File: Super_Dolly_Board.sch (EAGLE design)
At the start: 101 parts, among them J1 10118193-0001LF, J3 SJ1-2503A, J4 RJHSE-5381, J5 SJ1-2503A, J6 SJ1-2503A, P1 TC33X-2, SW1 SKQUDBE010, U1 AT90USB646-MU, U10 IP4234CZ6, U11 AT90USB646-AU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

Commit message: working on SDB REV4
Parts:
- added AUX_2: (no value), PP_Connectors:PH_1X081.27MM_PTH
- R3, R32, R6: value 10K -> 4.7K
- U$1: REVNUM 3 -> 4
- renumbered AUX to AUX_1
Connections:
- new net N$2: AUX_2.3
- net +5V: now also AUX_2.1
- net GND: now also AUX_2.2; no longer CG10.1
- net M0_A: now also U1.PA0(AD0), U11.PA0(AD0); no longer U1.PA3(AD3), U11.PA3(AD3)
- net M0_B: now also U1.PA1(AD1), U11.PA1(AD1); no longer U1.PA4(AD4), U11.PA4(AD4)
- net M0_P: now also U1.PA2(AD2), U11.PA2(AD2); no longer U1.PA0(AD0), U11.PA0(AD0)
- net M1_A: now also U1.PA3(AD3), U11.PA3(AD3); no longer U1.PA5(AD5), U11.PA5(AD5)
- net M1_B: now also U1.PA4(AD4), U11.PA4(AD4); no longer U1.PA6(AD6), U11.PA6(AD6)
- net M1_P: now also U1.PA5(AD5), U11.PA5(AD5); no longer U1.PA1(AD1), U11.PA1(AD1)
- net M2_A: now also U1.PA6(AD6), U11.PA6(AD6); no longer U1.PA7(AD7), U11.PA7(AD7)
- net M2_B: now also U1.PA7(AD7), U11.PA7(AD7); no longer U1.PB0(SS/PCINT0), U11.PB0(SS/PCINT0)
- net M2_P: now also U1.PB0(SS/PCINT0), U11.PB0(SS/PCINT0); no longer U1.PA2(AD2), U11.PA2(AD2)
- net PD5: now also AUX_2.4
- net PD6: now also AUX_2.5
- net PD7: now also AUX_2.6
- net PE0: now also AUX_2.7
- net PE1: now also AUX_2.8
- net PF5: now also U3.ST
- net PF6: now also U7.ST
- net PF7: now also U5.ST
- net UGND: now also CG10.1

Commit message: working on REv 4 of SDB
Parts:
- removed C20: 10uF, SparkFun:CAP_POL1206
- removed U9: TS2937CW50, SparkFun-PowerIC:V_REG_MIC2920
- added C22, C23: .1uF, parkers_parts:CAP_NONPOL0402
- added R35: 20K, parkers_parts:RESISTOR0402
- added R36: LRF1206-LF-R006JT, PP_Passives:RESISTOR1206
- added R37: 10K, parkers_parts:RESISTOR0402
- added U12: BSO080P03NS3E G, PP_DiscreteSemi:MOSFET_P-CHANNEL_SINGLEP3-POWER
- added U8: LMP8640MK-H/NOPB, PP_AnalogIC:LMP8640TSOT-6
- D1: value PMEG6010EP -> MMSZ5240C-V-GS08; device parkers_parts:DIODESOD-128 -> parkers_parts:DIODESOD-123
- D2: value PMEG6010EP -> PMEG4010EP,115
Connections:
- new net N$1: R35.2, U8.VOUT
- new net N$3: D1.ANODE, R37.2, U12.GATE
- new net VIN_J: PWR.PIN, U12.DRAIN
- new net VIN_M: C10.2, C11.2, C12.POS, C9.2, R36.2, U3.VS, U5.VS, U7.VS, U8.-IN
- net +5V: now also C22.2, U8.V+; no longer U9.OUT
- net 12VB: now also D2.ANODE; no longer C20.+, D2.CATHODE, U9.IN
- net GND: now also C22.1, C23.1, R37.1, U8.V-; no longer C20.-, D1.ANODE, D2.ANODE, U9.GND
- net PF2: now also C23.2, R35.1
- net PF5: no longer U3.ST
- net PF6: no longer U7.ST
- net PF7: no longer U5.ST
- net VIN: now also D2.CATHODE, R36.1, U12.SOURCE, U8.+IN; no longer C10.2, C11.2, C12.POS, C9.2, PWR.PIN, U3.VS, U5.VS, U7.VS
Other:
- moved on the sheet: C12, C16, C17, C18, C8, D1, D2, PWR, U4

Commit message: added a new PP_Sensor library and more parts to the datasheets
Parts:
- removed AUX_1: (no value), pinhead:PINHD-2X4
- added U13, U14, U9: MCP9701T-E/TT, PP_Sensors:MCP970XSOT-23-3
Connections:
- removed net BATT_V: C14.1, R4.2, R5.1, U1.PF1(ADC1), U11.PF1(ADC1)
- removed net PF2: AUX_1.3, C23.2, R35.1, U1.PF2(ADC2), U11.PF2(ADC2)
- removed net PF3: AUX_1.4, U1.PF3(ADC3), U11.PF3(ADC3)
- removed net PF4: AUX_1.5, U1.PF4(ADC4/TCK), U11.PF4(ADC4/TCK)
- removed net PF5: AUX_1.6, U1.PF5(ADC5/TMS), U11.PF5(ADC5/TMS)
- new net CUR_SENSOR: C23.2, R35.1, U1.PF1(ADC1), U11.PF1(ADC1)
- new net TEMP0_SENSOR: U1.PF5(ADC5/TMS), U11.PF5(ADC5/TMS), U9.VOUT
- new net TEMP1_SENSOR: U1.PF4(ADC4/TCK), U11.PF4(ADC4/TCK), U13.VOUT
- new net TEMP2_SENSOR: U1.PF3(ADC3), U11.PF3(ADC3), U14.VOUT
- new net VOL_SENSOR: C14.1, R4.2, R5.1, U1.PF2(ADC2), U11.PF2(ADC2)
- net +5V: now also U13.VDD, U14.VDD, U9.VDD; no longer AUX_1.1
- net GND: now also U13.GND, U14.GND, U9.GND; no longer AUX_1.2
- net PF6: no longer AUX_1.7
- net PF7: no longer AUX_1.8

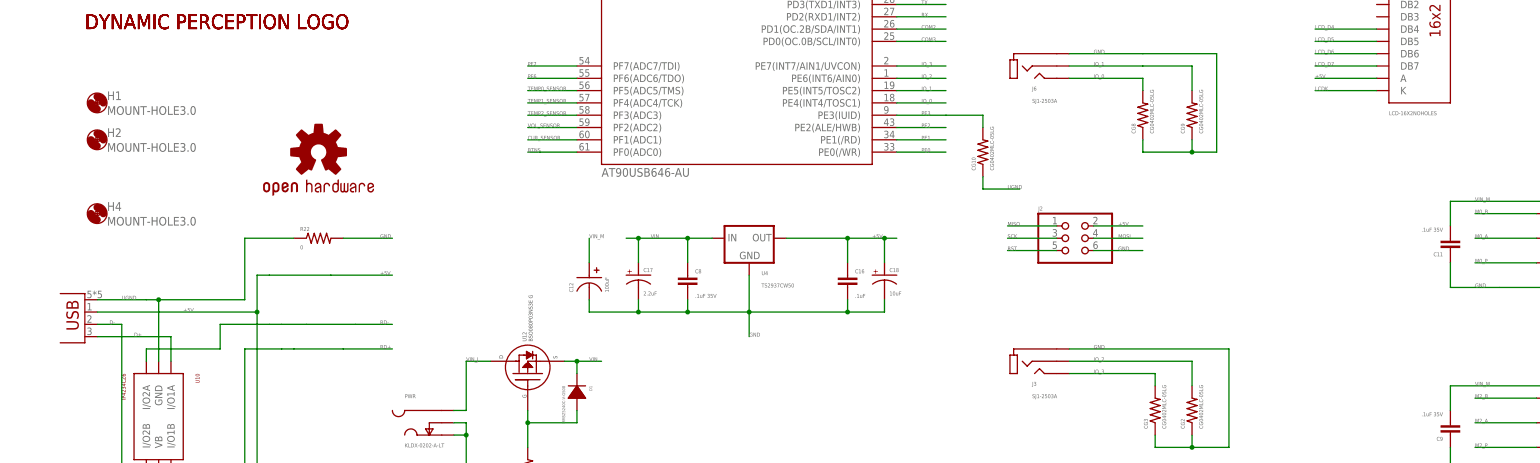
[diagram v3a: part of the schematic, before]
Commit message: REV4 of SDB complete. added 2 parts to datasheets and libraires.
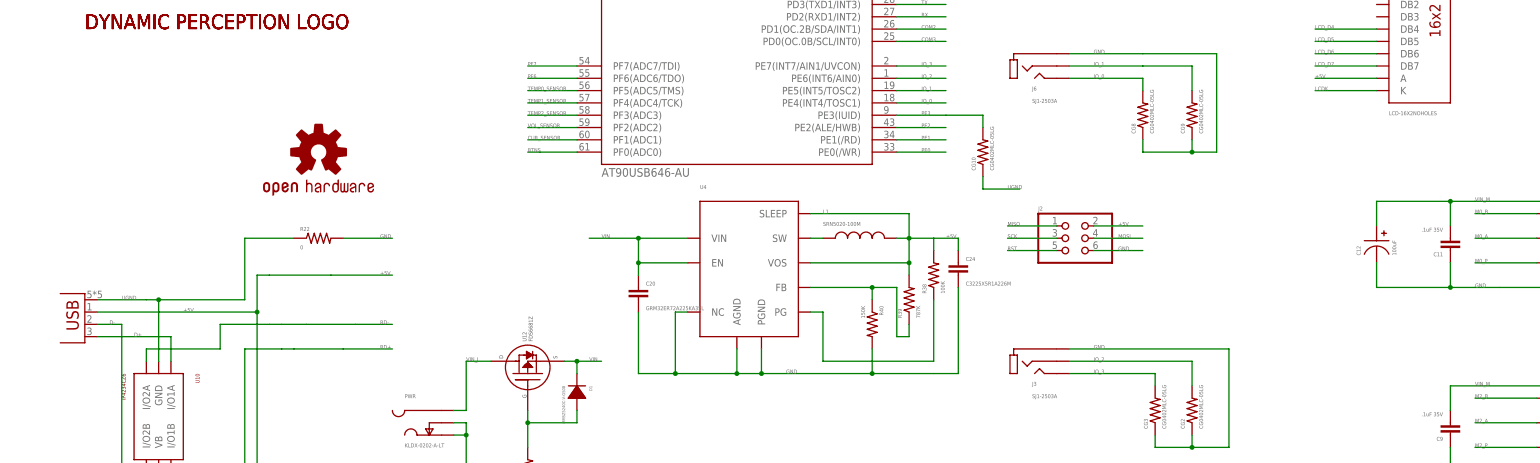
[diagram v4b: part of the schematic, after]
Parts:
- removed C16: .1uF, parkers_parts:CAP_NONPOL0402
- removed C17: 2.2uF, SparkFun:CAP_POL1206
- removed C18: 10uF, SparkFun:CAP_POL1206
- removed C8: .1uF 35V, parkers_parts:CAP_NONPOL0402
- removed H1, H2, H4: MOUNT-HOLE3.0, holes:MOUNT-HOLE3.0
- added C20: GRM32ER72A225KA35L, PP_Passives:CAPACITOR_NON_POLAR1206
- added C24: C3225X5R1A226M, PP_Passives:CAPACITOR_NON_POLAR1206
- added L1: SRN5020-100M, PP_Passives:INDUCTORSRN5020
- added R38: 100K, PP_Passives:RESISTOR0402
- added R39: 787K, PP_Passives:RESISTOR0402
- added R40: 150K, PP_Passives:RESISTOR0402
- U12: value BSO080P03NS3E G -> FDS6681Z
- U4: value TS2937CW50 -> (none); device SparkFun-PowerIC:V_REG_MIC2920 -> PP_DigitalIC:TPS6217XWSON-10
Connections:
- new net N$11: R38.1, U4.PG
- new net N$13: L1.P$1, U4.SW
- new net N$14: R39.1, R40.1, U4.FB
- net +5V: now also C24.1, L1.P$2, R38.2, R39.2, U4.SLEEP, U4.VOS; no longer C16.1, C18.+, U4.OUT
- net GND: now also C20.2, C24.2, R40.2, U4.AGND, U4.NC, U4.PGND; no longer C16.2, C17.-, C18.-, C8.2, U4.GND
- net VIN: now also C20.1, U4.EN, U4.VIN; no longer C17.+, C8.1, U4.IN
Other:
- moved on the sheet: C12

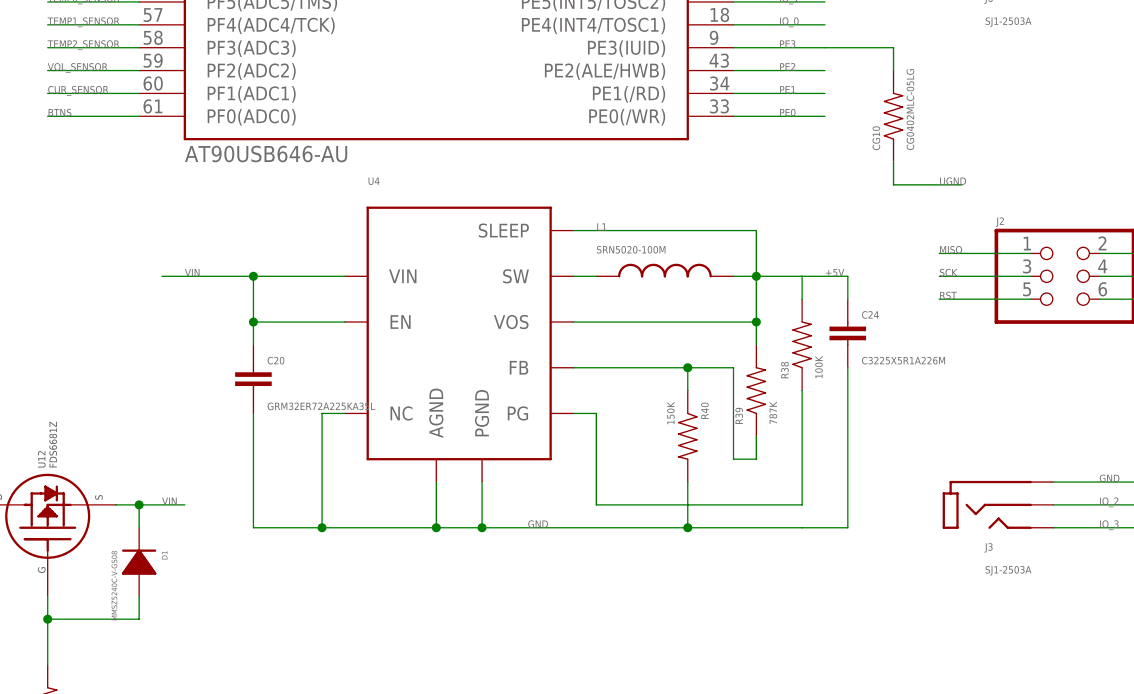
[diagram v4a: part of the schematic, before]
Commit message: added a part to PP_poweric and replaced the switcher regulator with a linear one.
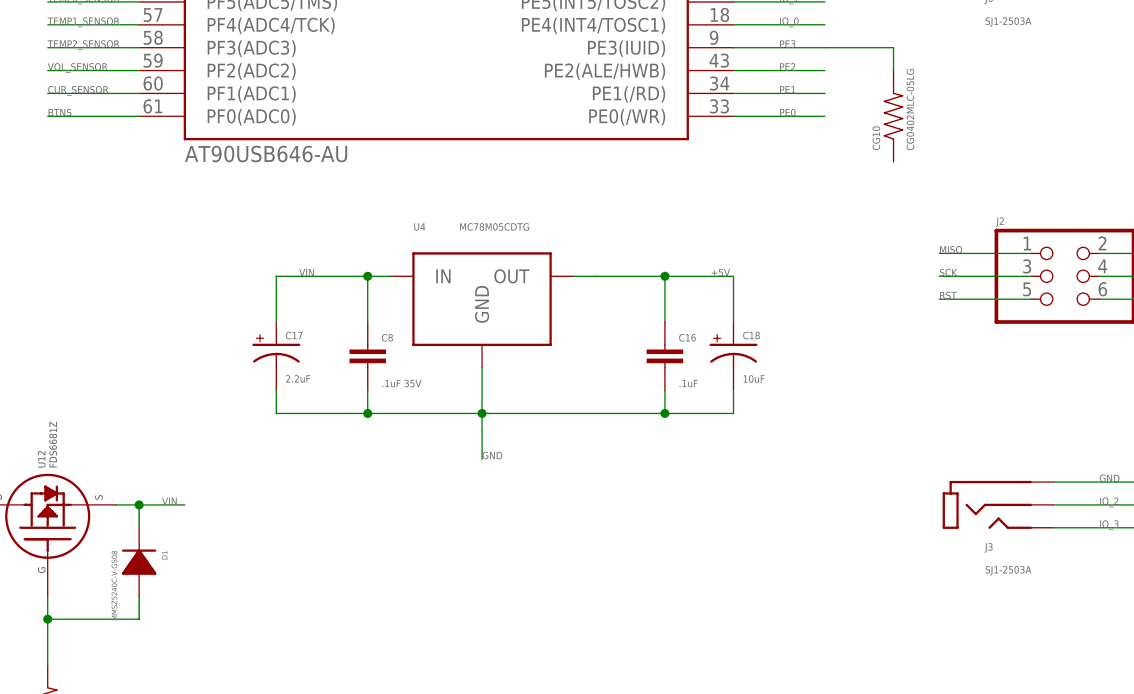
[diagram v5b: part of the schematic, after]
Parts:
- removed C20: GRM32ER72A225KA35L, PP_Passives:CAPACITOR_NON_POLAR1206
- removed C24: C3225X5R1A226M, PP_Passives:CAPACITOR_NON_POLAR1206
- removed L1: SRN5020-100M, PP_Passives:INDUCTORSRN5020
- removed R38: 100K, PP_Passives:RESISTOR0402
- removed R39: 787K, PP_Passives:RESISTOR0402
- removed R40: 150K, PP_Passives:RESISTOR0402
- added C16: .1uF, parkers_parts:CAP_NONPOL0402
- added C17: 2.2uF, SparkFun:CAP_POL1206
- added C18: 10uF, SparkFun:CAP_POL1206
- added C8: .1uF 35V, parkers_parts:CAP_NONPOL0402
- U4: value (none) -> MC78M05CDTG; device PP_DigitalIC:TPS6217XWSON-10 -> PP_PowerIC:FIXED_VOLTAGE_REGDPAK-3
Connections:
- removed net N$11: R38.1, U4.PG
- removed net N$13: L1.P$1, U4.SW
- removed net N$14: R39.1, R40.1, U4.FB
- net +5V: now also C16.1, C18.+, U4.OUT; no longer C24.1, L1.P$2, R38.2, R39.2, U4.SLEEP, U4.VOS
- net GND: now also C16.2, C17.-, C18.-, C8.2, U4.GND; no longer C20.2, C24.2, R40.2, U4.AGND, U4.NC, U4.PGND
- net UGND: no longer CG10.1
- net VIN: now also C17.+, C8.1, U4.IN; no longer C20.1, U4.EN, U4.VIN
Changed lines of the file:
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@@
 <part name="U13" library="PP_Sensors" deviceset="MCP970X" device="SOT-23-3" value="MCP9701T-E/TT"/>
 <part name="U14" library="PP_Sensors" deviceset="MCP970X" device="SOT-23-3" value="MCP9701T-E/TT"/>
-<part name="U4" library="PP_DigitalIC" deviceset="TPS6217X" device="WSON-10"/>
-<part name="C20" library="PP_Passives" deviceset="CAPACITOR_NON_POLAR" device="1206" value="GRM32ER72A225KA35L"/>
-<part name="C24" library="PP_Passives" deviceset="CAPACITOR_NON_POLAR" device="1206" value="C3225X5R1A226M"/>
-<part name="L1" library="PP_Passives" deviceset="INDUCTOR" device="SRN5020" value="SRN5020-100M"/>
-<part name="R38" library="PP_Passives" deviceset="RESISTOR" device="0402" value="100K"/>
-<part name="R39" library="PP_Passives" deviceset="RESISTOR" device="0402" value="787K"/>
-<part name="R40" library="PP_Passives" deviceset="RESISTOR" device="0402" value="150K"/>
+<part name="C8" library="parkers_parts" deviceset="CAP_NONPOL" device="0402" value=".1uF 35V"/>
+<part name="C16" library="parkers_parts" deviceset="CAP_NONPOL" device="0402" value=".1uF"/>
+<part name="C17" library="SparkFun" deviceset="CAP_POL" device="1206" value="2.2uF"/>
+<part name="C18" library="SparkFun" deviceset="CAP_POL" device="1206" value="10uF"/>
+<part name="U4" library="PP_PowerIC" deviceset="FIXED_VOLTAGE_REG" device="DPAK-3" value="MC78M05CDTG"/>
 </parts>
 <sheets>
@@
 <instance part="U13" gate="G$1" x="396.24" y="15.24"/>
 <instance part="U14" gate="G$1" x="396.24" y="-2.54"/>
-<instance part="U4" gate="G$1" x="25.4" y="2.54"/>
-<instance part="C20" gate="G$1" x="5.08" y="5.08"/>
-<instance part="C24" gate="G$1" x="71.12" y="10.16"/>
-<instance part="L1" gate="G$1" x="50.8" y="15.24"/>
-<instance part="R38" gate="G$1" x="66.04" y="7.62" rot="R90"/>
-<instance part="R39" gate="G$1" x="60.96" y="2.54" rot="R90"/>
-<instance part="R40" gate="G$1" x="53.34" y="-2.54" rot="R270"/>
+<instance part="C8" gate="G$1" x="17.78" y="7.62"/>
+<instance part="C16" gate="G$1" x="50.8" y="7.62"/>
+<instance part="C17" gate="G$1" x="7.62" y="7.62" smashed="yes">
+<attribute name="NAME" x="8.636" y="8.255" size="0.8128" layer="95"/>
+<attribute name="VALUE" x="8.636" y="3.429" size="0.8128" layer="96"/>
+</instance>
+<instance part="C18" gate="G$1" x="58.42" y="7.62" smashed="yes">
+<attribute name="NAME" x="59.436" y="8.255" size="0.8128" layer="95"/>
+<attribute name="VALUE" x="59.436" y="3.429" size="0.8128" layer="96"/>
+</instance>
+<instance part="U4" gate="G$1" x="30.48" y="15.24"/>
 </instances>
 <busses>
@@
 </segment>
 <segment>
-<pinref part="L1" gate="G$1" pin="P$2"/>
-<wire x1="58.42" y1="15.24" x2="60.96" y2="15.24" width="0.1524" layer="91"/>
-<pinref part="C24" gate="G$1" pin="1"/>
-<wire x1="60.96" y1="15.24" x2="66.04" y2="15.24" width="0.1524" layer="91"/>
-<wire x1="66.04" y1="15.24" x2="71.12" y2="15.24" width="0.1524" layer="91"/>
-<wire x1="71.12" y1="15.24" x2="71.12" y2="12.7" width="0.1524" layer="91"/>
-<label x="68.58" y="15.24" size="0.8128" layer="95" font="vector"/>
-<pinref part="U4" gate="G$1" pin="SLEEP"/>
-<wire x1="40.64" y1="20.32" x2="60.96" y2="20.32" width="0.1524" layer="91"/>
-<wire x1="60.96" y1="20.32" x2="60.96" y2="15.24" width="0.1524" layer="91"/>
-<junction x="60.96" y="15.24"/>
-<pinref part="U4" gate="G$1" pin="VOS"/>
-<wire x1="40.64" y1="10.16" x2="60.96" y2="10.16" width="0.1524" layer="91"/>
-<wire x1="60.96" y1="10.16" x2="60.96" y2="15.24" width="0.1524" layer="91"/>
-<pinref part="R38" gate="G$1" pin="2"/>
-<wire x1="66.04" y1="12.7" x2="66.04" y2="15.24" width="0.1524" layer="91"/>
-<pinref part="R39" gate="G$1" pin="2"/>
-<wire x1="60.96" y1="7.62" x2="60.96" y2="10.16" width="0.1524" layer="91"/>
-<junction x="60.96" y="10.16"/>
+<label x="55.88" y="15.24" size="0.8128" layer="95"/>
+<pinref part="C16" gate="G$1" pin="1"/>
+<wire x1="50.8" y1="15.24" x2="58.42" y2="15.24" width="0.1524" layer="91"/>
+<wire x1="50.8" y1="10.16" x2="50.8" y2="15.24" width="0.1524" layer="91"/>
+<pinref part="C18" gate="G$1" pin="+"/>
+<wire x1="58.42" y1="10.16" x2="58.42" y2="15.24" width="0.1524" layer="91"/>
+<wire x1="43.18" y1="15.24" x2="50.8" y2="15.24" width="0.1524" layer="91"/>
+<pinref part="U4" gate="G$1" pin="OUT"/>
+<wire x1="43.18" y1="15.24" x2="40.64" y2="15.24" width="0.1524" layer="91"/>
+<junction x="50.8" y="15.24"/>
 </segment>
 </net>
@@
 </segment>
 <segment>
-<pinref part="U4" gate="G$1" pin="AGND"/>
-<wire x1="25.4" y1="-7.62" x2="25.4" y2="-12.7" width="0.1524" layer="91"/>
-<wire x1="25.4" y1="-12.7" x2="30.48" y2="-12.7" width="0.1524" layer="91"/>
-<pinref part="U4" gate="G$1" pin="PGND"/>
-<wire x1="30.48" y1="-12.7" x2="30.48" y2="-7.62" width="0.1524" layer="91"/>
-<label x="35.56" y="-12.7" size="0.8128" layer="95" font="vector"/>
-<pinref part="U4" gate="G$1" pin="NC"/>
-<wire x1="15.24" y1="0" x2="12.7" y2="0" width="0.1524" layer="91"/>
-<wire x1="12.7" y1="0" x2="12.7" y2="-12.7" width="0.1524" layer="91"/>
-<wire x1="12.7" y1="-12.7" x2="25.4" y2="-12.7" width="0.1524" layer="91"/>
-<junction x="25.4" y="-12.7"/>
-<pinref part="C20" gate="G$1" pin="2"/>
-<wire x1="5.08" y1="0" x2="5.08" y2="-12.7" width="0.1524" layer="91"/>
-<wire x1="5.08" y1="-12.7" x2="12.7" y2="-12.7" width="0.1524" layer="91"/>
-<junction x="12.7" y="-12.7"/>
-<pinref part="C24" gate="G$1" pin="2"/>
-<wire x1="71.12" y1="5.08" x2="71.12" y2="-12.7" width="0.1524" layer="91"/>
-<wire x1="71.12" y1="-12.7" x2="66.04" y2="-12.7" width="0.1524" layer="91"/>
-<junction x="30.48" y="-12.7"/>
-<wire x1="66.04" y1="-12.7" x2="53.34" y2="-12.7" width="0.1524" layer="91"/>
-<pinref part="R40" gate="G$1" pin="2"/>
-<wire x1="53.34" y1="-12.7" x2="30.48" y2="-12.7" width="0.1524" layer="91"/>
-<wire x1="53.34" y1="-7.62" x2="53.34" y2="-12.7" width="0.1524" layer="91"/>
-<junction x="53.34" y="-12.7"/>
+<label x="30.48" y="-5.08" size="0.8128" layer="95"/>
+<pinref part="C8" gate="G$1" pin="2"/>
+<wire x1="30.48" y1="0" x2="30.48" y2="-5.08" width="0.1524" layer="91"/>
+<wire x1="17.78" y1="2.54" x2="17.78" y2="0" width="0.1524" layer="91"/>
+<wire x1="17.78" y1="0" x2="30.48" y2="0" width="0.1524" layer="91"/>
+<pinref part="C16" gate="G$1" pin="2"/>
+<wire x1="30.48" y1="0" x2="50.8" y2="0" width="0.1524" layer="91"/>
+<wire x1="50.8" y1="0" x2="50.8" y2="2.54" width="0.1524" layer="91"/>
+<junction x="30.48" y="0"/>
+<pinref part="C17" gate="G$1" pin="-"/>
+<wire x1="7.62" y1="2.54" x2="7.62" y2="0" width="0.1524" layer="91"/>
+<wire x1="7.62" y1="0" x2="17.78" y2="0" width="0.1524" layer="91"/>
+<junction x="17.78" y="0"/>
+<pinref part="C18" gate="G$1" pin="-"/>
+<wire x1="50.8" y1="0" x2="58.42" y2="0" width="0.1524" layer="91"/>
+<wire x1="58.42" y1="0" x2="58.42" y2="2.54" width="0.1524" layer="91"/>
+<junction x="50.8" y="0"/>
+<pinref part="U4" gate="G$1" pin="GND"/>
+<wire x1="30.48" y1="5.08" x2="30.48" y2="0" width="0.1524" layer="91"/>
 </segment>
 </net>
@@
 </segment>
 <segment>
-<pinref part="U4" gate="G$1" pin="VIN"/>
-<wire x1="15.24" y1="15.24" x2="5.08" y2="15.24" width="0.1524" layer="91"/>
-<pinref part="U4" gate="G$1" pin="EN"/>
-<pinref part="C20" gate="G$1" pin="1"/>
-<wire x1="5.08" y1="15.24" x2="-5.08" y2="15.24" width="0.1524" layer="91"/>
-<wire x1="15.24" y1="10.16" x2="5.08" y2="10.16" width="0.1524" layer="91"/>
-<wire x1="5.08" y1="10.16" x2="5.08" y2="7.62" width="0.1524" layer="91"/>
-<wire x1="5.08" y1="15.24" x2="5.08" y2="10.16" width="0.1524" layer="91"/>
-<junction x="5.08" y="10.16"/>
-<junction x="5.08" y="15.24"/>
-<label x="-2.54" y="15.24" size="0.8128" layer="95" font="vector"/>
+<label x="10.16" y="15.24" size="0.8128" layer="95"/>
+<pinref part="C8" gate="G$1" pin="1"/>
+<wire x1="17.78" y1="15.24" x2="7.62" y2="15.24" width="0.1524" layer="91"/>
+<wire x1="17.78" y1="10.16" x2="17.78" y2="15.24" width="0.1524" layer="91"/>
+<pinref part="C17" gate="G$1" pin="+"/>
+<wire x1="7.62" y1="10.16" x2="7.62" y2="15.24" width="0.1524" layer="91"/>
+<pinref part="U4" gate="G$1" pin="IN"/>
+<wire x1="17.78" y1="15.24" x2="20.32" y2="15.24" width="0.1524" layer="91"/>
+<junction x="17.78" y="15.24"/>
 </segment>
 </net>
@@
 <label x="454.66" y="48.26" size="0.8128" layer="95" font="vector"/>
 </segment>
-<segment>
-<pinref part="CG10" gate="G$1" pin="1"/>
-<wire x1="76.2" y1="27.94" x2="76.2" y2="25.4" width="0.1524" layer="91"/>
-<wire x1="76.2" y1="25.4" x2="83.82" y2="25.4" width="0.1524" layer="91"/>
-<label x="81.28" y="25.4" size="0.8128" layer="95" font="vector"/>
-</segment>
 </net>
 <net name="PF7" class="0">
@@
 </segment>
 </net>
-<net name="N$13" class="0">
-<segment>
-<pinref part="U4" gate="G$1" pin="SW"/>
-<pinref part="L1" gate="G$1" pin="P$1"/>
-<wire x1="40.64" y1="15.24" x2="43.18" y2="15.24" width="0.1524" layer="91"/>
-</segment>
-</net>
-<net name="N$11" class="0">
-<segment>
-<pinref part="U4" gate="G$1" pin="PG"/>
-<wire x1="40.64" y1="0" x2="43.18" y2="0" width="0.1524" layer="91"/>
-<wire x1="43.18" y1="0" x2="43.18" y2="-10.16" width="0.1524" layer="91"/>
-<pinref part="R38" gate="G$1" pin="1"/>
-<wire x1="43.18" y1="-10.16" x2="66.04" y2="-10.16" width="0.1524" layer="91"/>
-<wire x1="66.04" y1="-10.16" x2="66.04" y2="2.54" width="0.1524" layer="91"/>
-</segment>
-</net>
-<net name="N$14" class="0">
-<segment>
-<pinref part="R40" gate="G$1" pin="1"/>
-<wire x1="53.34" y1="2.54" x2="53.34" y2="5.08" width="0.1524" layer="91"/>
-<pinref part="U4" gate="G$1" pin="FB"/>
-<wire x1="53.34" y1="5.08" x2="40.64" y2="5.08" width="0.1524" layer="91"/>
-<pinref part="R39" gate="G$1" pin="1"/>
-<wire x1="60.96" y1="-2.54" x2="60.96" y2="-5.08" width="0.1524" layer="91"/>
-<wire x1="60.96" y1="-5.08" x2="58.42" y2="-5.08" width="0.1524" layer="91"/>
-<wire x1="58.42" y1="-5.08" x2="58.42" y2="5.08" width="0.1524" layer="91"/>
-<wire x1="58.42" y1="5.08" x2="53.34" y2="5.08" width="0.1524" layer="91"/>
-<junction x="53.34" y="5.08"/>
-</segment>
-</net>
